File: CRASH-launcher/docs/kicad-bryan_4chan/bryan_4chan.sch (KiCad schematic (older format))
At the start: 0 parts

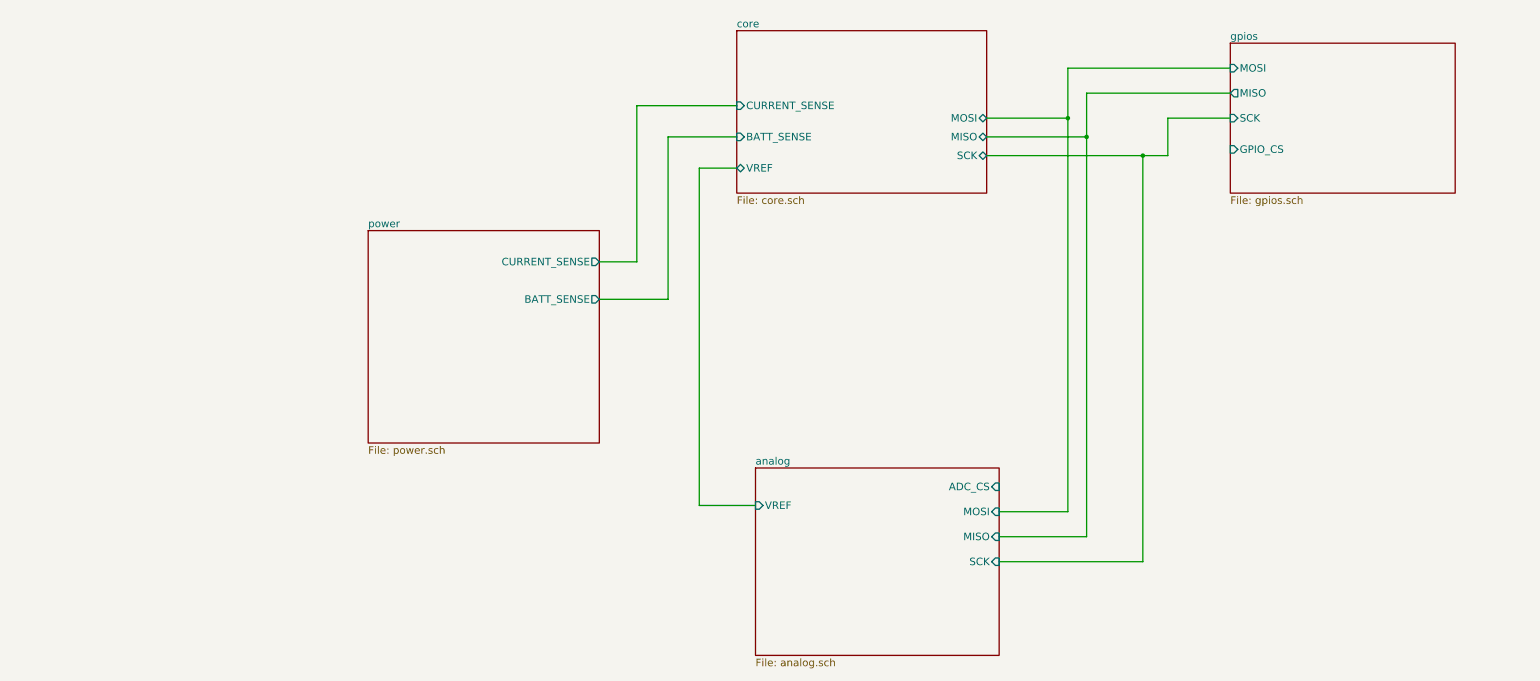
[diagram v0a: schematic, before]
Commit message: 
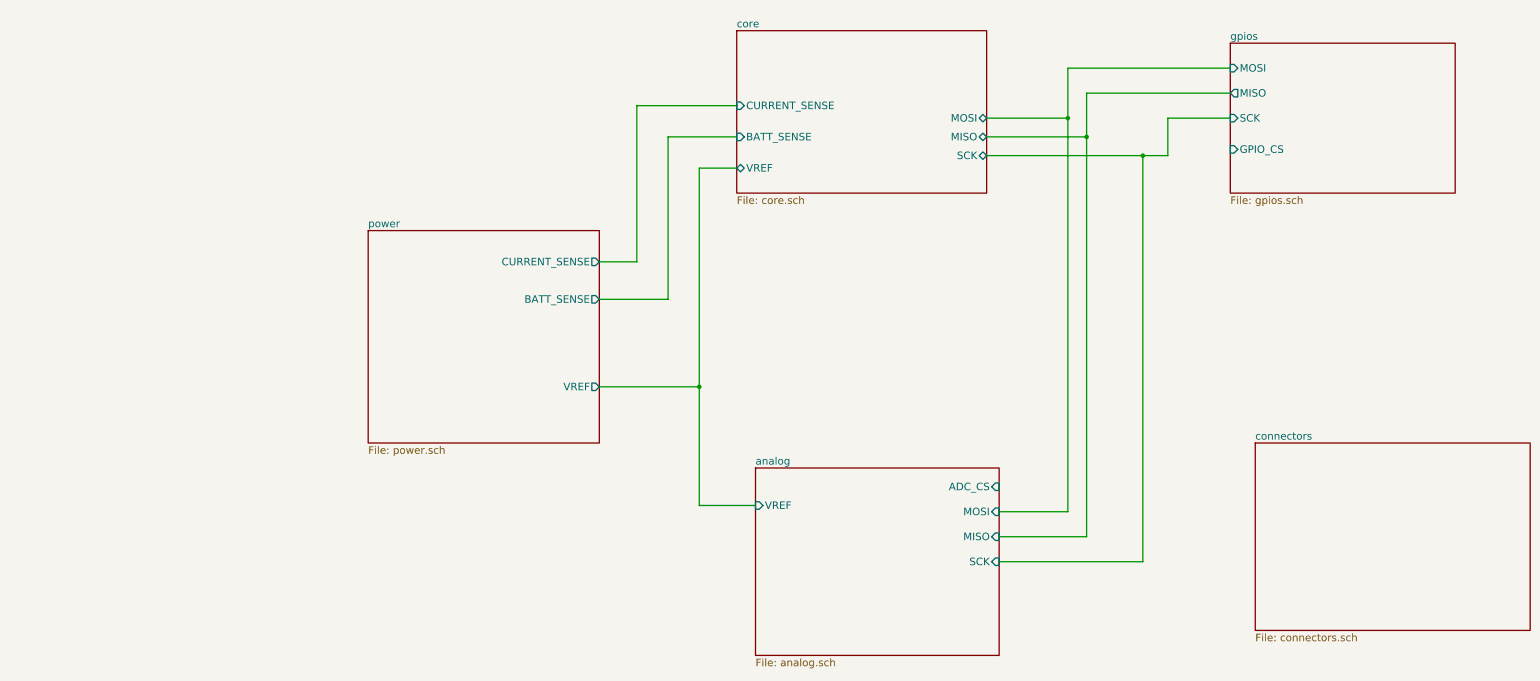
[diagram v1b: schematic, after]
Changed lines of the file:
@@
-EESchema Schematic File Version 2  date Mon 20 Feb 2012 05:21:35 PM MST
+EESchema Schematic File Version 2  date Sat 05 May 2012 12:12:20 AM MDT
 LIBS:bryan_custom
 LIBS:rfm12
@@
 $Descr User 11000 8500
 encoding utf-8
-Sheet 1 5
+Sheet 1 6
 Title ""
-Date "21 feb 2012"
+Date "13 apr 2012"
 Rev ""
 Comp ""
@@
 $EndDescr
 Wire Wire Line
-	4100 4950 3650 4950
+	2850 3300 3400 3300
 Wire Wire Line
-	3650 4950 3650 2250
+	3400 3300 3400 2000
 Wire Wire Line
-	3650 2250 3950 2250
+	3400 2000 3950 2000
+Connection ~ 6600 1850
 Wire Wire Line
-	2850 3000 3150 3000
+	6050 5000 6600 5000
 Wire Wire Line
-	3150 3000 3150 1750
+	6600 5000 6600 1450
+Connection ~ 7200 2150
 Wire Wire Line
-	3150 1750 3950 1750
-Connection ~ 6750 2000
+	6050 5400 7200 5400
 Wire Wire Line
-	6750 5200 6750 1650
+	7200 5400 7200 2150
 Wire Wire Line
-	6750 5200 6050 5200
+	7900 1850 7400 1850
 Wire Wire Line
-	7900 1450 6600 1450
+	7400 1850 7400 2150
+Wire Wire Line
+	7400 2150 5950 2150
+Wire Wire Line
+	7900 1650 6750 1650
+Wire Wire Line
+	5950 2000 6750 2000
 Wire Wire Line
 	6600 1850 5950 1850
 Wire Wire Line
-	5950 2000 6750 2000
+	6600 1450 7900 1450
 Wire Wire Line
-	6750 1650 7900 1650
+	6050 5200 6750 5200
 Wire Wire Line
-	5950 2150 7400 2150
+	6750 5200 6750 1650
+Connection ~ 6750 2000
 Wire Wire Line
-	7400 2150 7400 1850
+	3950 1750 3150 1750
 Wire Wire Line
-	7400 1850 7900 1850
+	3150 1750 3150 3000
 Wire Wire Line
-	7200 2150 7200 5400
+	3150 3000 2850 3000
 Wire Wire Line
-	7200 5400 6050 5400
-Connection ~ 7200 2150
+	3950 2250 3650 2250
 Wire Wire Line
-	6600 1450 6600 5000
+	3650 2250 3650 4950
 Wire Wire Line
-	6600 5000 6050 5000
-Connection ~ 6600 1850
+	3650 4950 4100 4950
 Wire Wire Line
-	3950 2000 3400 2000
-Wire Wire Line
-	3400 2000 3400 3300
-Wire Wire Line
-	3400 3300 2850 3300
+	2850 4000 3650 4000
+Connection ~ 3650 4000
+$Sheet
+S 8100 4450 2200 1500
+U 4F865AA5
+F0 "connectors" 60
+F1 "connectors.sch" 60
+$EndSheet
 $Sheet
 S 1000 2750 1850 1700
@@
 F2 "CURRENT_SENSE" O R 2850 3000 60
 F3 " BATT_SENSE" O R 2850 3300 60
+F4 "VREF" O R 2850 4000 60
 $EndSheet
 $Sheet

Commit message: first REAL shot at PCB
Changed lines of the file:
@@
-EESchema Schematic File Version 2  date Sat 05 May 2012 12:12:20 AM MDT
+EESchema Schematic File Version 2  date Fri 08 Jun 2012 10:29:21 PM MDT
 LIBS:bryan_custom
 LIBS:rfm12
@@
 Sheet 1 6
 Title ""
-Date "13 apr 2012"
+Date "8 jun 2012"
 Rev ""
 Comp ""
@@
 $EndDescr
 Wire Wire Line
-	2850 3300 3400 3300
+	7900 1250 5950 1250
 Wire Wire Line
-	3400 3300 3400 2000
+	6050 4800 6250 4800
 Wire Wire Line
-	3400 2000 3950 2000
-Connection ~ 6600 1850
+	6250 4800 6250 2300
 Wire Wire Line
-	6050 5000 6600 5000
+	6250 2300 5950 2300
+Connection ~ 3650 4000
 Wire Wire Line
-	6600 5000 6600 1450
-Connection ~ 7200 2150
+	2850 4000 3650 4000
 Wire Wire Line
-	6050 5400 7200 5400
+	4100 4950 3650 4950
 Wire Wire Line
-	7200 5400 7200 2150
+	3650 4950 3650 2250
 Wire Wire Line
-	7900 1850 7400 1850
+	3650 2250 3950 2250
 Wire Wire Line
-	7400 1850 7400 2150
+	2850 3000 3150 3000
 Wire Wire Line
-	7400 2150 5950 2150
+	3150 3000 3150 1750
 Wire Wire Line
-	7900 1650 6750 1650
+	3150 1750 3950 1750
+Connection ~ 6750 2000
+Wire Wire Line
+	6750 5200 6750 1650
+Wire Wire Line
+	6750 5200 6050 5200
+Wire Wire Line
+	7900 1450 6600 1450
+Wire Wire Line
+	6600 1850 5950 1850
 Wire Wire Line
 	5950 2000 6750 2000
 Wire Wire Line
-	6600 1850 5950 1850
+	6750 1650 7900 1650
 Wire Wire Line
-	6600 1450 7900 1450
+	5950 2150 7400 2150
 Wire Wire Line
-	6050 5200 6750 5200
+	7400 2150 7400 1850
 Wire Wire Line
-	6750 5200 6750 1650
-Connection ~ 6750 2000
+	7400 1850 7900 1850
 Wire Wire Line
-	3950 1750 3150 1750
+	7200 2150 7200 5400
 Wire Wire Line
-	3150 1750 3150 3000
+	7200 5400 6050 5400
+Connection ~ 7200 2150
 Wire Wire Line
-	3150 3000 2850 3000
+	6600 1450 6600 5000
 Wire Wire Line
-	3950 2250 3650 2250
+	6600 5000 6050 5000
+Connection ~ 6600 1850
 Wire Wire Line
-	3650 2250 3650 4950
+	3950 2000 3400 2000
 Wire Wire Line
-	3650 4950 4100 4950
+	3400 2000 3400 3300
 Wire Wire Line
-	2850 4000 3650 4000
-Connection ~ 3650 4000
+	3400 3300 2850 3300
+Connection ~ -1850 1250
 $Sheet
 S 8100 4450 2200 1500
@@
 $EndSheet
 $Sheet
-S 7900 1250 1800 1200
+S 7900 1100 1800 1200
 U 4F25C482
 F0 "gpios" 60
@@
 F3 "MOSI" I L 7900 1450 60
 F4 "MISO" O L 7900 1650 60
-F5 "GPIO_CS" I L 7900 2100 60
+F5 "GPIO_CS" I L 7900 1250 60
 $EndSheet
 $Sheet
@@
 F6 "MISO" B R 5950 2000 60
 F7 "SCK" B R 5950 2150 60
+F8 "GPIO_CS" O R 5950 1250 60
+F9 "ADC_CS" O R 5950 2300 60
 $EndSheet
 $EndSCHEMATC

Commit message: second try at PCB layout.  this one might actually work!
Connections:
- no-connect marks 0 -> 1
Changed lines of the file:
@@
-EESchema Schematic File Version 2  date Fri 08 Jun 2012 10:29:21 PM MDT
+EESchema Schematic File Version 2  date Sun 10 Jun 2012 01:48:40 AM MDT
 LIBS:bryan_custom
 LIBS:rfm12
@@
 Sheet 1 6
 Title ""
-Date "8 jun 2012"
+Date "10 jun 2012"
 Rev ""
 Comp ""
@@
 Comment4 ""
 $EndDescr
+NoConn ~ 4950 1500
 Wire Wire Line
-	7900 1250 5950 1250
+	5950 1400 7900 1400
 Wire Wire Line
-	6050 4800 6250 4800
+	2850 3300 3400 3300
 Wire Wire Line
-	6250 4800 6250 2300
+	3400 3300 3400 2000
 Wire Wire Line
-	6250 2300 5950 2300
-Connection ~ 3650 4000
+	3400 2000 3950 2000
+Connection ~ 6600 1850
 Wire Wire Line
-	2850 4000 3650 4000
+	6050 5000 6600 5000
 Wire Wire Line
-	4100 4950 3650 4950
+	6600 5000 6600 1550
+Connection ~ 7200 2150
 Wire Wire Line
-	3650 4950 3650 2250
+	6050 5400 7200 5400
 Wire Wire Line
-	3650 2250 3950 2250
+	7200 5400 7200 2150
 Wire Wire Line
-	2850 3000 3150 3000
+	7900 1850 7400 1850
 Wire Wire Line
-	3150 3000 3150 1750
+	7400 1850 7400 2150
 Wire Wire Line
-	3150 1750 3950 1750
-Connection ~ 6750 2000
+	7400 2150 5950 2150
 Wire Wire Line
-	6750 5200 6750 1650
+	7900 1650 6750 1650
 Wire Wire Line
-	6750 5200 6050 5200
-Wire Wire Line
-	7900 1450 6600 1450
+	5950 2000 6750 2000
 Wire Wire Line
 	6600 1850 5950 1850
 Wire Wire Line
-	5950 2000 6750 2000
+	6600 1550 7900 1550
 Wire Wire Line
-	6750 1650 7900 1650
+	6050 5200 6750 5200
 Wire Wire Line
-	5950 2150 7400 2150
+	6750 5200 6750 1650
+Connection ~ 6750 2000
 Wire Wire Line
-	7400 2150 7400 1850
+	3950 1750 3150 1750
 Wire Wire Line
-	7400 1850 7900 1850
+	3150 1750 3150 3000
 Wire Wire Line
-	7200 2150 7200 5400
+	3150 3000 2850 3000
 Wire Wire Line
-	7200 5400 6050 5400
-Connection ~ 7200 2150
+	3950 2250 3650 2250
 Wire Wire Line
-	6600 1450 6600 5000
+	3650 2250 3650 4950
 Wire Wire Line
-	6600 5000 6050 5000
-Connection ~ 6600 1850
+	3650 4950 4100 4950
 Wire Wire Line
-	3950 2000 3400 2000
+	2850 4000 3650 4000
+Connection ~ 3650 4000
 Wire Wire Line
-	3400 2000 3400 3300
+	5950 2300 6250 2300
 Wire Wire Line
-	3400 3300 2850 3300
-Connection ~ -1850 1250
+	6250 2300 6250 4800
+Wire Wire Line
+	6250 4800 6050 4800
+Wire Wire Line
+	7900 1250 5950 1250
 $Sheet
 S 8100 4450 2200 1500
@@
 F1 "gpios.sch" 60
 F2 "SCK" I L 7900 1850 60
-F3 "MOSI" I L 7900 1450 60
+F3 "MOSI" I L 7900 1550 60
 F4 "MISO" O L 7900 1650 60
 F5 "GPIO_CS" I L 7900 1250 60
+F6 "GPIO_RESET" I L 7900 1400 60
 $EndSheet
 $Sheet
@@
 F8 "GPIO_CS" O R 5950 1250 60
 F9 "ADC_CS" O R 5950 2300 60
+F10 "GPIO_RESET" O R 5950 1400 60
 $EndSheet
 $EndSCHEMATC

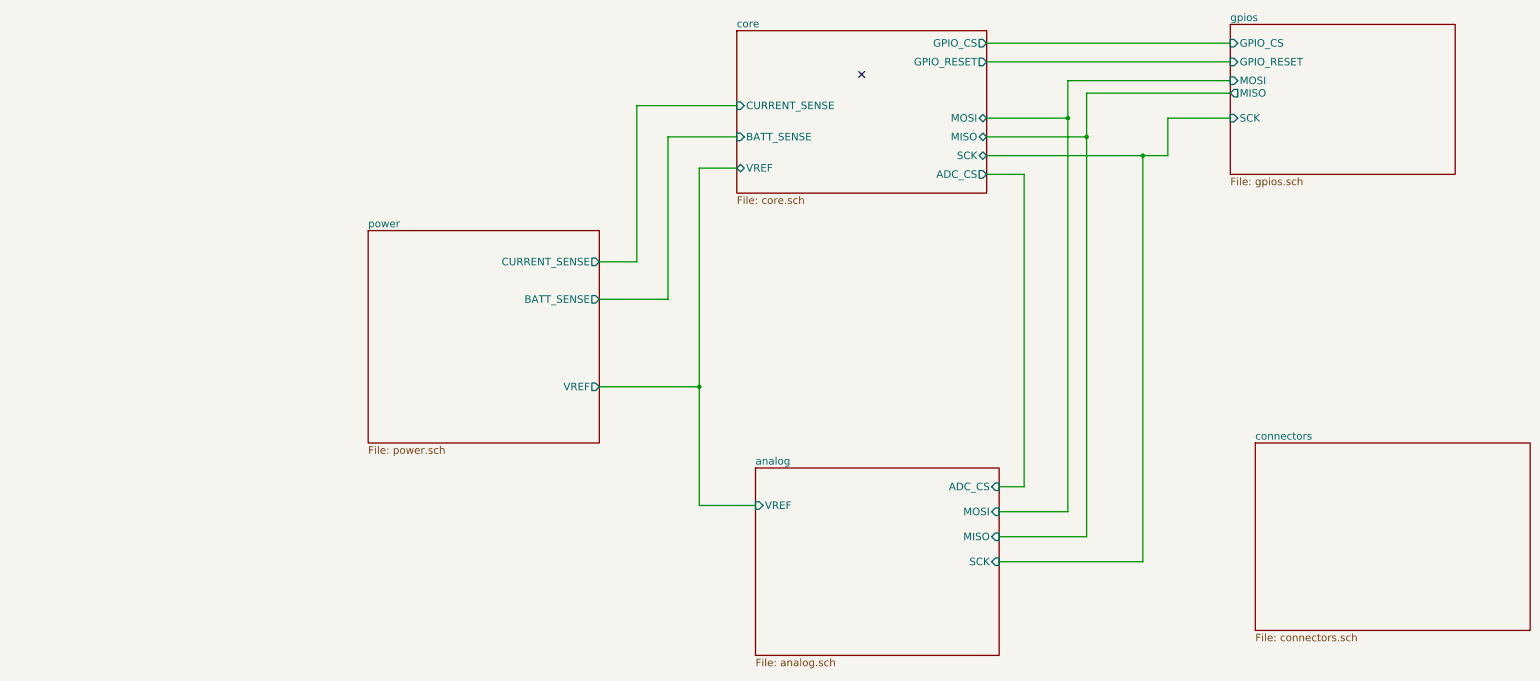
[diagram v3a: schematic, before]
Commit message: further refined PCB, it has safety switch and fire switch and lots of errors fixed!
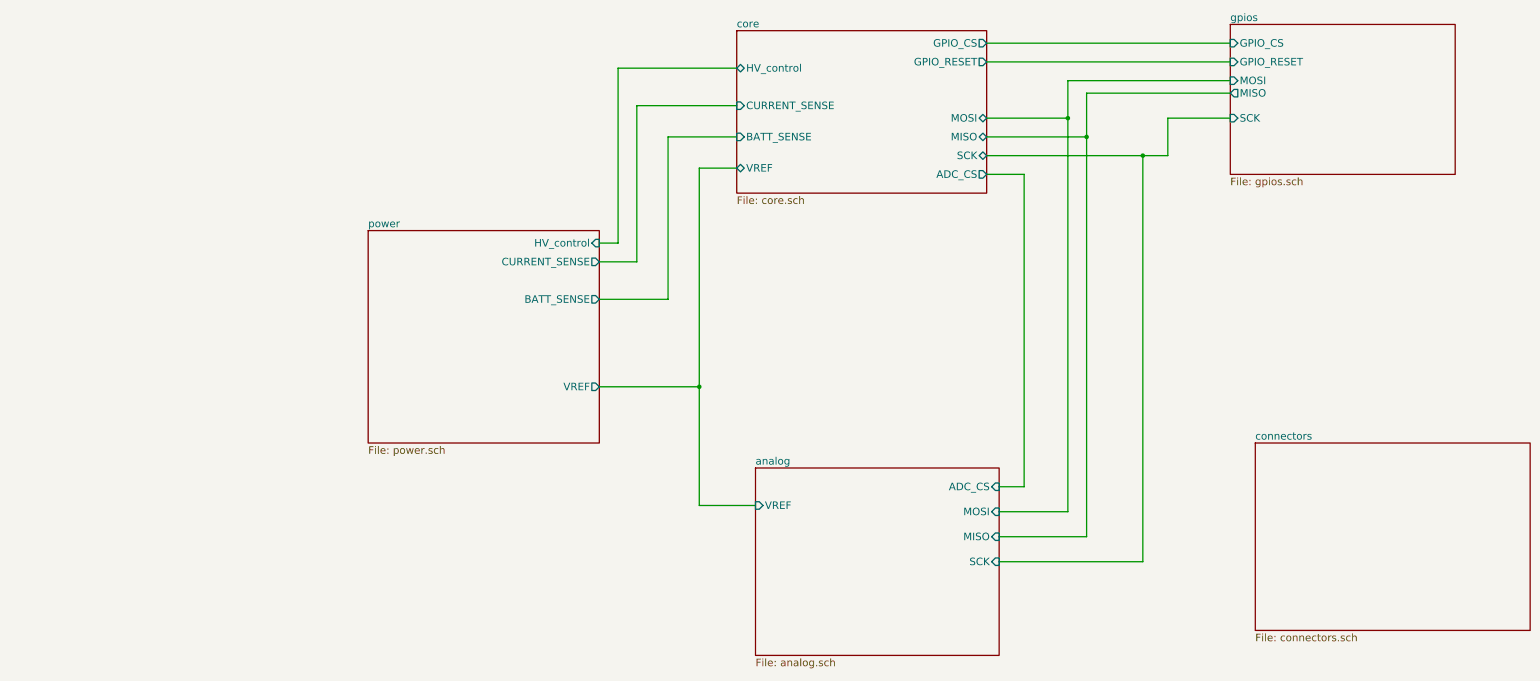
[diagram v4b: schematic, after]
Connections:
- no-connect marks 1 -> 0
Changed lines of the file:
@@
-EESchema Schematic File Version 2  date Sun 10 Jun 2012 01:48:40 AM MDT
+EESchema Schematic File Version 2  date Sun 10 Jun 2012 11:49:54 PM MDT
 LIBS:bryan_custom
 LIBS:rfm12
@@
 Sheet 1 6
 Title ""
-Date "10 jun 2012"
+Date "11 jun 2012"
 Rev ""
 Comp ""
@@
 Comment4 ""
 $EndDescr
-NoConn ~ 4950 1500
 Wire Wire Line
-	5950 1400 7900 1400
+	2850 2850 3000 2850
 Wire Wire Line
-	2850 3300 3400 3300
+	3000 2850 3000 1450
 Wire Wire Line
-	3400 3300 3400 2000
+	3000 1450 3950 1450
 Wire Wire Line
-	3400 2000 3950 2000
-Connection ~ 6600 1850
+	7900 1250 5950 1250
 Wire Wire Line
-	6050 5000 6600 5000
+	6050 4800 6250 4800
 Wire Wire Line
-	6600 5000 6600 1550
-Connection ~ 7200 2150
+	6250 4800 6250 2300
 Wire Wire Line
-	6050 5400 7200 5400
+	6250 2300 5950 2300
+Connection ~ 3650 4000
 Wire Wire Line
-	7200 5400 7200 2150
+	2850 4000 3650 4000
 Wire Wire Line
-	7900 1850 7400 1850
+	4100 4950 3650 4950
 Wire Wire Line
-	7400 1850 7400 2150
+	3650 4950 3650 2250
 Wire Wire Line
-	7400 2150 5950 2150
+	3650 2250 3950 2250
 Wire Wire Line
-	7900 1650 6750 1650
+	2850 3000 3150 3000
+Wire Wire Line
+	3150 3000 3150 1750
+Wire Wire Line
+	3150 1750 3950 1750
+Connection ~ 6750 2000
+Wire Wire Line
+	6750 5200 6750 1650
+Wire Wire Line
+	6750 5200 6050 5200
+Wire Wire Line
+	7900 1550 6600 1550
+Wire Wire Line
+	6600 1850 5950 1850
 Wire Wire Line
 	5950 2000 6750 2000
 Wire Wire Line
-	6600 1850 5950 1850
+	6750 1650 7900 1650
 Wire Wire Line
-	6600 1550 7900 1550
+	5950 2150 7400 2150
 Wire Wire Line
-	6050 5200 6750 5200
+	7400 2150 7400 1850
 Wire Wire Line
-	6750 5200 6750 1650
-Connection ~ 6750 2000
+	7400 1850 7900 1850
 Wire Wire Line
-	3950 1750 3150 1750
+	7200 2150 7200 5400
 Wire Wire Line
-	3150 1750 3150 3000
+	7200 5400 6050 5400
+Connection ~ 7200 2150
 Wire Wire Line
-	3150 3000 2850 3000
+	6600 1550 6600 5000
 Wire Wire Line
-	3950 2250 3650 2250
+	6600 5000 6050 5000
+Connection ~ 6600 1850
 Wire Wire Line
-	3650 2250 3650 4950
+	3950 2000 3400 2000
 Wire Wire Line
-	3650 4950 4100 4950
+	3400 2000 3400 3300
 Wire Wire Line
-	2850 4000 3650 4000
-Connection ~ 3650 4000
+	3400 3300 2850 3300
 Wire Wire Line
-	5950 2300 6250 2300
-Wire Wire Line
-	6250 2300 6250 4800
-Wire Wire Line
-	6250 4800 6050 4800
-Wire Wire Line
-	7900 1250 5950 1250
+	5950 1400 7900 1400
 $Sheet
 S 8100 4450 2200 1500
@@
 F3 " BATT_SENSE" O R 2850 3300 60
 F4 "VREF" O R 2850 4000 60
+F5 "HV_control" I R 2850 2850 60
 $EndSheet
 $Sheet
@@
 F9 "ADC_CS" O R 5950 2300 60
 F10 "GPIO_RESET" O R 5950 1400 60
+F11 "HV_control" B L 3950 1450 60
 $EndSheet
 $EndSCHEMATC
